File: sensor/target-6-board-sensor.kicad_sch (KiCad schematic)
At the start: 8 parts, among them J1 RJ25

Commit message: sensor: change buzzer to 15mm from 12mm
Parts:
- BZ1: footprint Buzzer_Beeper:Buzzer_12x9.5RM7.6 -> Buzzer_Beeper:Buzzer_15x7.5RM7.6
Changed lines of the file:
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@@
       (effects (font (size 1.27 1.27)) (justify left))
     )
-    (property "Footprint" "Buzzer_Beeper:Buzzer_12x9.5RM7.6" (at 34.925 78.74 90)
+    (property "Footprint" "Buzzer_Beeper:Buzzer_15x7.5RM7.6" (at 34.925 78.74 90)
       (effects (font (size 1.27 1.27)) hide)
     )

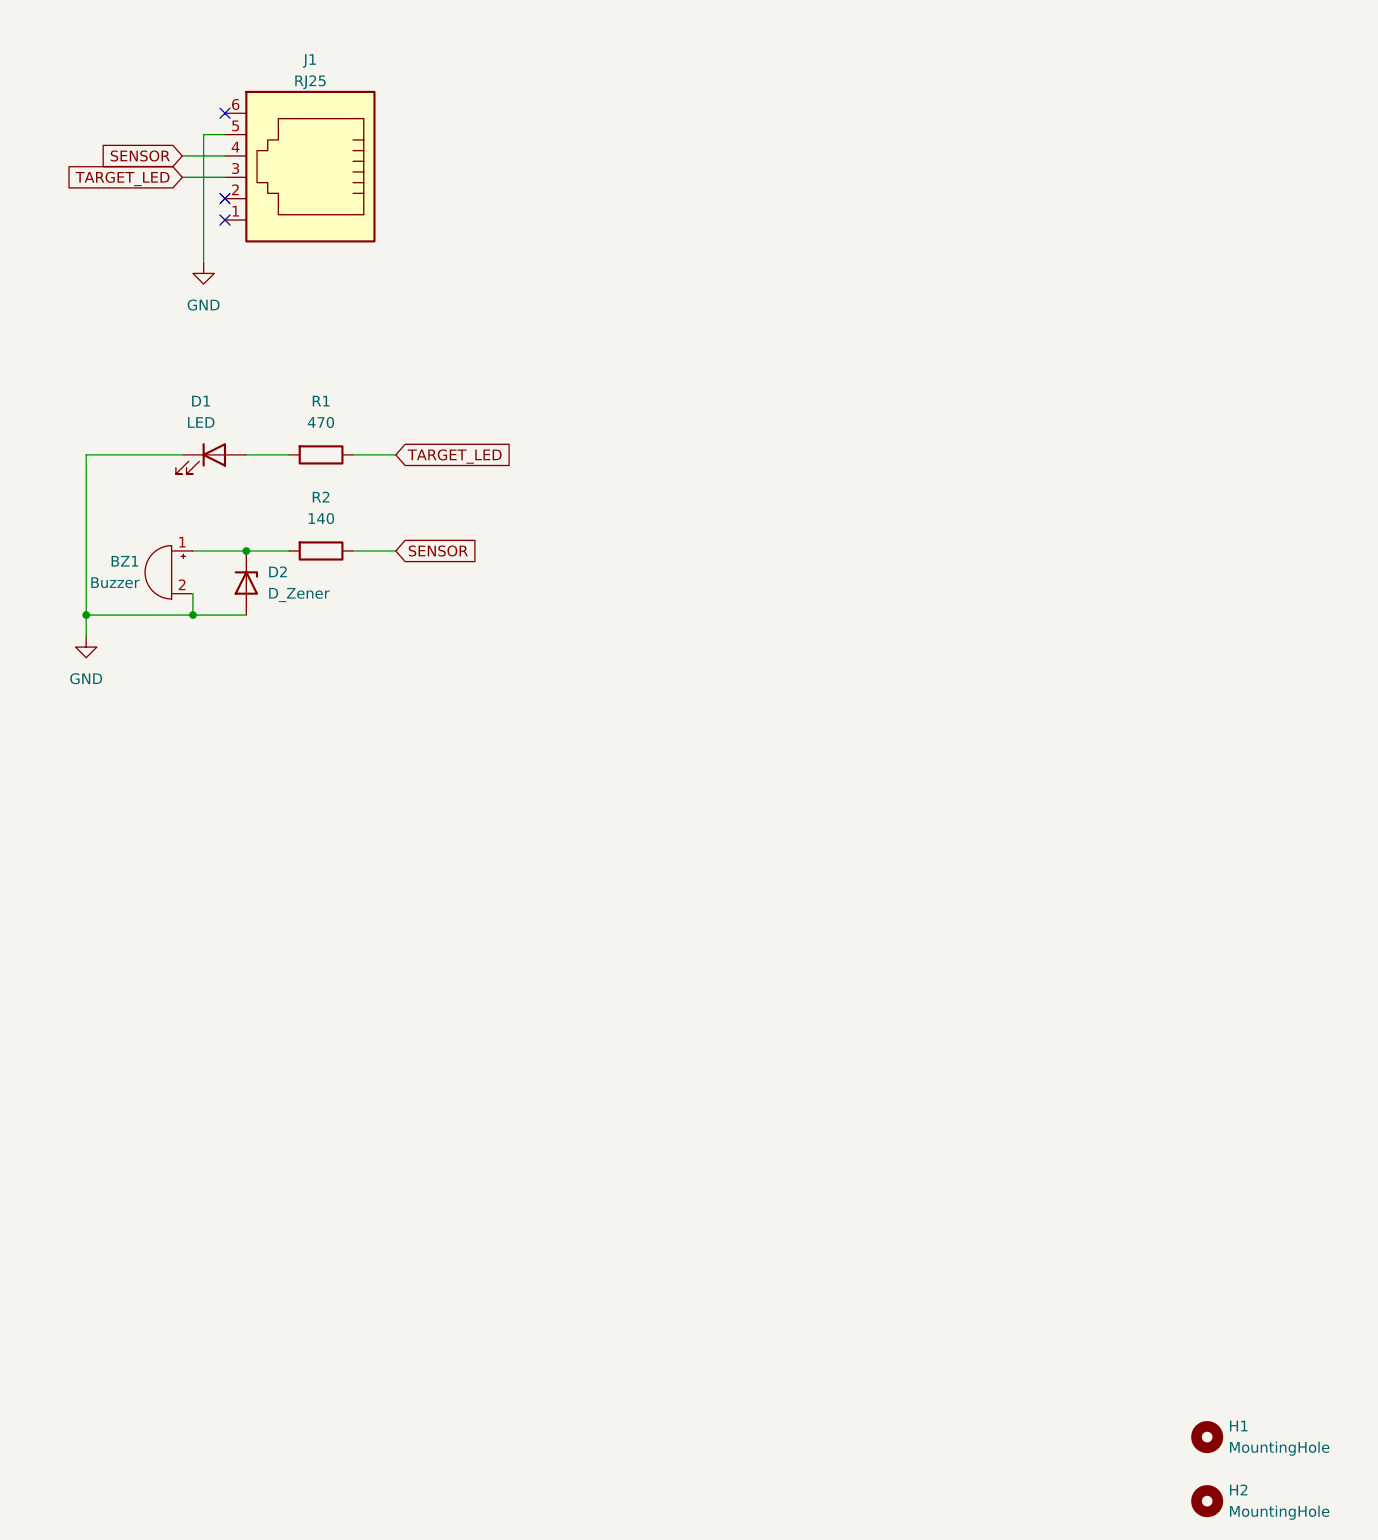
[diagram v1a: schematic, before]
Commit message: sensor: fix distance of mounting holes
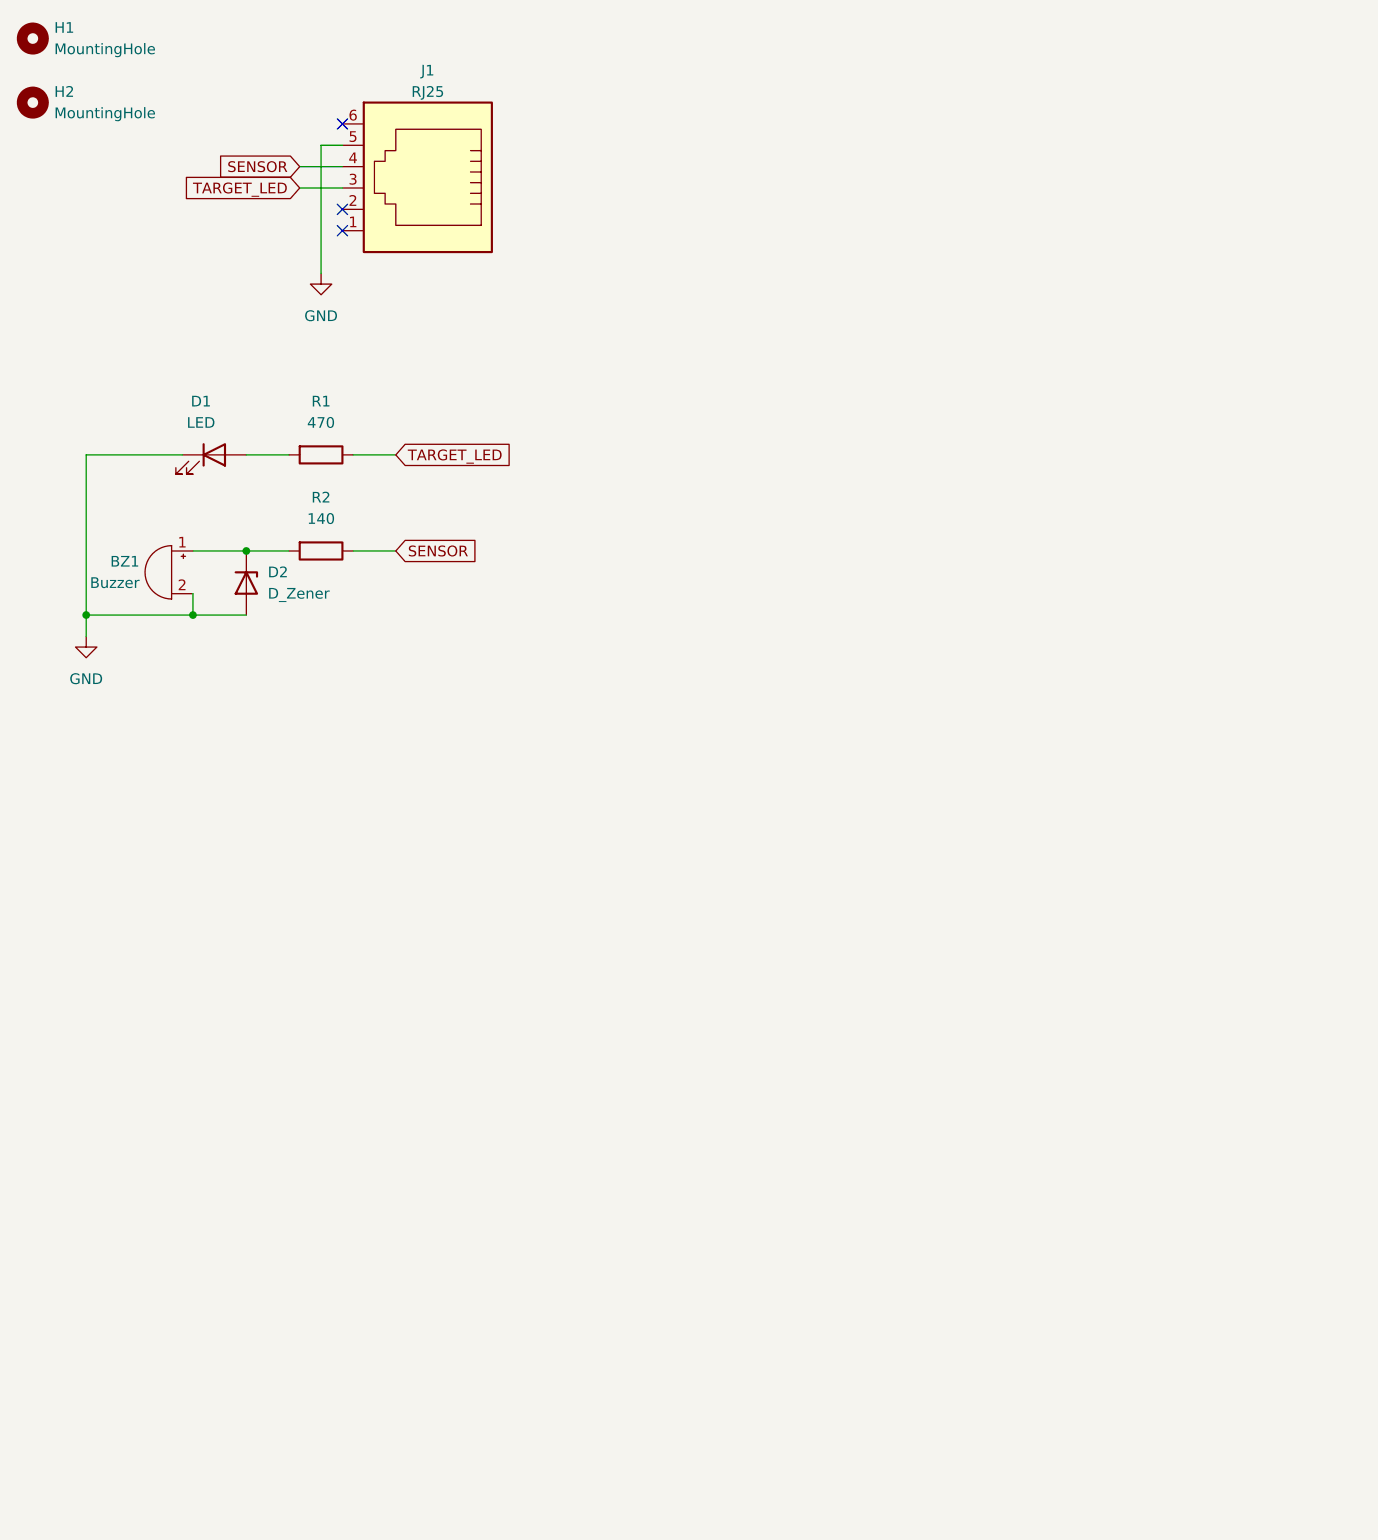
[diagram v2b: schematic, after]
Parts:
- H1, H2: footprint MountingHole:MountingHole_3.2mm_M3 -> MountingHole:MountingHole_2.2mm_M2
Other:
- moved on the sheet: H1, H2, J1
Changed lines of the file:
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@@
   (junction (at 43.18 78.74) (diameter 0) (color 0 0 0 0)
   )
-  (no_connect (at 40.64 36.83))
-  (no_connect (at 40.64 26.67))
-  (no_connect (at 40.64 39.37))
+  (no_connect (at 54.61 38.1))
+  (no_connect (at 54.61 27.94))
+  (no_connect (at 54.61 40.64))
   (wire (pts (xy 55.88 78.74) (xy 60.96 78.74))
     (stroke (width 0) (type default))
@@
     (stroke (width 0) (type default))
   )
-  (wire (pts (xy 38.1 29.21) (xy 40.64 29.21))
+  (wire (pts (xy 52.07 30.48) (xy 54.61 30.48))
     (stroke (width 0) (type default))
   )
@@
     (stroke (width 0) (type default))
   )
-  (wire (pts (xy 35.56 34.29) (xy 40.64 34.29))
-    (stroke (width 0) (type default))
-  )
-  (wire (pts (xy 38.1 29.21) (xy 38.1 44.45))
+  (wire (pts (xy 49.53 35.56) (xy 54.61 35.56))
+    (stroke (width 0) (type default))
+  )
+  (wire (pts (xy 52.07 30.48) (xy 52.07 45.72))
     (stroke (width 0) (type default))
   )
@@
     (stroke (width 0) (type default))
   )
-  (wire (pts (xy 35.56 31.75) (xy 40.64 31.75))
+  (wire (pts (xy 49.53 33.02) (xy 54.61 33.02))
     (stroke (width 0) (type default))
   )
@@
     )
   )
-  (global_label "SENSOR" (shape input) (at 35.56 31.75 180) (fields_autoplaced)
+  (global_label "SENSOR" (shape input) (at 49.53 33.02 180) (fields_autoplaced)
     (effects (font (size 1.27 1.27)) (justify right))
-    (property "Intersheetrefs" "${INTERSHEET_REFS}" (at 25.0758 31.75 0)
+    (property "Intersheetrefs" "${INTERSHEET_REFS}" (at 39.0458 33.02 0)
       (effects (font (size 1.27 1.27)) (justify right) hide)
     )
   )
-  (global_label "TARGET_LED" (shape input) (at 35.56 34.29 180) (fields_autoplaced)
+  (global_label "TARGET_LED" (shape input) (at 49.53 35.56 180) (fields_autoplaced)
     (effects (font (size 1.27 1.27)) (justify right))
-    (property "Intersheetrefs" "${INTERSHEET_REFS}" (at 21.4473 34.29 0)
+    (property "Intersheetrefs" "${INTERSHEET_REFS}" (at 35.4173 35.56 0)
       (effects (font (size 1.27 1.27)) (justify right) hide)
     )
   )
-  (symbol (lib_id "power:GND") (at 38.1 44.45 0) (unit 1)
-    (in_bom yes) (on_board yes) (dnp no) (fields_autoplaced)
-    (property "Reference" "#PWR01" (at 38.1 50.8 0)
-      (effects (font (size 1.27 1.27)) hide)
-    )
-    (property "Value" "GND" (at 38.1 49.53 0)
-      (effects (font (size 1.27 1.27)))
-    )
-    (property "Footprint" "" (at 38.1 44.45 0)
-      (effects (font (size 1.27 1.27)) hide)
-    )
-    (property "Datasheet" "" (at 38.1 44.45 0)
+  (symbol (lib_id "power:GND") (at 52.07 45.72 0) (unit 1)
+    (in_bom yes) (on_board yes) (dnp no) (fields_autoplaced)
+    (property "Reference" "#PWR01" (at 52.07 52.07 0)
+      (effects (font (size 1.27 1.27)) hide)
+    )
+    (property "Value" "GND" (at 52.07 50.8 0)
+      (effects (font (size 1.27 1.27)))
+    )
+    (property "Footprint" "" (at 52.07 45.72 0)
+      (effects (font (size 1.27 1.27)) hide)
+    )
+    (property "Datasheet" "" (at 52.07 45.72 0)
       (effects (font (size 1.27 1.27)) hide)
     )
@@
     )
   )
-  (symbol (lib_id "Connector:RJ25") (at 50.8 34.29 0) (mirror y) (unit 1)
+  (symbol (lib_id "Connector:RJ25") (at 64.77 35.56 0) (mirror y) (unit 1)
     (in_bom yes) (on_board yes) (dnp no)
-    (property "Reference" "J1" (at 50.8 20.32 0)
-      (effects (font (size 1.27 1.27)))
-    )
-    (property "Value" "RJ25" (at 50.8 22.86 0)
-      (effects (font (size 1.27 1.27)))
-    )
-    (property "Footprint" "Connector_RJ:RJ25_Wayconn_MJEA-660X1_Horizontal" (at 50.8 33.655 90)
-      (effects (font (size 1.27 1.27)) hide)
-    )
-    (property "Datasheet" "~" (at 50.8 33.655 90)
+    (property "Reference" "J1" (at 64.77 21.59 0)
+      (effects (font (size 1.27 1.27)))
+    )
+    (property "Value" "RJ25" (at 64.77 24.13 0)
+      (effects (font (size 1.27 1.27)))
+    )
+    (property "Footprint" "Connector_RJ:RJ25_Wayconn_MJEA-660X1_Horizontal" (at 64.77 34.925 90)
+      (effects (font (size 1.27 1.27)) hide)
+    )
+    (property "Datasheet" "~" (at 64.77 34.925 90)
       (effects (font (size 1.27 1.27)) hide)
     )
@@
     )
   )
-  (symbol (lib_id "Mechanical:MountingHole") (at 157.48 191.77 0) (unit 1)
-    (in_bom yes) (on_board yes) (dnp no) (fields_autoplaced)
-    (property "Reference" "H2" (at 160.02 190.5 0)
-      (effects (font (size 1.27 1.27)) (justify left))
-    )
-    (property "Value" "MountingHole" (at 160.02 193.04 0)
-      (effects (font (size 1.27 1.27)) (justify left))
-    )
-    (property "Footprint" "MountingHole:MountingHole_3.2mm_M3" (at 157.48 191.77 0)
-      (effects (font (size 1.27 1.27)) hide)
-    )
-    (property "Datasheet" "~" (at 157.48 191.77 0)
+  (symbol (lib_id "Mechanical:MountingHole") (at 17.78 25.4 0) (unit 1)
+    (in_bom yes) (on_board yes) (dnp no) (fields_autoplaced)
+    (property "Reference" "H2" (at 20.32 24.13 0)
+      (effects (font (size 1.27 1.27)) (justify left))
+    )
+    (property "Value" "MountingHole" (at 20.32 26.67 0)
+      (effects (font (size 1.27 1.27)) (justify left))
+    )
+    (property "Footprint" "MountingHole:MountingHole_2.2mm_M2" (at 17.78 25.4 0)
+      (effects (font (size 1.27 1.27)) hide)
+    )
+    (property "Datasheet" "~" (at 17.78 25.4 0)
       (effects (font (size 1.27 1.27)) hide)
     )
@@
     )
   )
-  (symbol (lib_id "Mechanical:MountingHole") (at 157.48 184.15 0) (unit 1)
-    (in_bom yes) (on_board yes) (dnp no) (fields_autoplaced)
-    (property "Reference" "H1" (at 160.02 182.88 0)
-      (effects (font (size 1.27 1.27)) (justify left))
-    )
-    (property "Value" "MountingHole" (at 160.02 185.42 0)
-      (effects (font (size 1.27 1.27)) (justify left))
-    )
-    (property "Footprint" "MountingHole:MountingHole_3.2mm_M3" (at 157.48 184.15 0)
-      (effects (font (size 1.27 1.27)) hide)
-    )
-    (property "Datasheet" "~" (at 157.48 184.15 0)
-      (effects (font (size 1.27 1.27)) hide)
-    )
+  (symbol (lib_id "Mechanical:MountingHole") (at 17.78 17.78 0) (unit 1)
+    (in_bom yes) (on_board yes) (dnp no) (fields_autoplaced)
+    (property "Reference" "H1" (at 20.32 16.51 0)
+      (effects (font (size 1.27 1.27)) (justify left))
+    )
+    (property "Value" "MountingHole" (at 20.32 19.05 0)
+      (effects (font (size 1.27 1.27)) (justify left))
+    )
+    (property "Footprint" "MountingHole:MountingHole_2.2mm_M2" (at 17.78 17.78 0)
+      (effects (font (size 1.27 1.27)) hide)
+    )
+    (property "Datasheet" "~" (at 17.78 17.78 0)
+      (effects (font (size 1.27 1.27)) hide)
+    )
